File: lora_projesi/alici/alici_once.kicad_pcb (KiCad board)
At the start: 4 copper layers, 88 x 102 mm, 127 parts, among them J1 USB-C, J2 SMA, J3 RJ45, J4 u.FL (ANA ANTEN), J5 12 V GIRIS, J6 LAMBA, J7 MICRO-SIM, J8 u.FL (YARDIMCI ANTEN, ISTEGE 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, K1 SRD-12VDC-SL-A, Q1 AO3401A, Q2 MMBT2222A, Q3 MMBT2222A, Q4 MMBT2222A, SW1 DUGME, U1 ESP32-S3-WROOM-1-N4, U10 SIM7600SA, U11 AP2112K-3.3, U12 ESDA6V1-5SC6, U4 RFM95W-915S2, U5 TPS62933DRLR, U6 TPS62933DRLR, U7 USBLC6-2SC6, U8 TXB0104PW, U9 W5500, Y1 25 MHz

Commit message: A7670SA, Ra-01H, LM66100 ideal diyot, SRP7028A, USBLC6-2: uretec ve kutuphane (kart yonlendirmesi suruyor)
Co-Authored-By: Claude Sonnet 5.5 <noreply@anthropic.com>
Claude-Session: https://claude.ai/code/session_01Q71gHQtKJ86ZE2CtYTYSwP
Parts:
- removed D4: SS14, D_SMA
- removed J8: u.FL (YARDIMCI ANTEN, ISTEGE BAGLI), U.FL_Hirose_U.FL-R-SMT-1_Vertical
- removed R36: 0, R_0603_1608Metric
- added C52: 33pF, C_0603_1608Metric, B.Cu at (37.8, 52.9)
- added C53: 10pF, C_0603_1608Metric, B.Cu at (41.7, 49.1)
- added C54: 1uF, C_0603_1608Metric, B.Cu at (43.6, 50.0)
- added R39: 22, R_0603_1608Metric, B.Cu at (17.8, 54.0)
- added R40: 22, R_0603_1608Metric, B.Cu at (16.0, 52.0)
- added R41: 22, R_0603_1608Metric, B.Cu at (15.1, 50.1)
- added TP4: USB_VBUS, TestPoint_Pad_1.0x1.0mm, F.Cu at (11.2, 47.6)
- added TP5: UART_LOG_TX, TestPoint_Pad_1.0x1.0mm, F.Cu at (10.6, 44.5)
- added U13: USBLC6-2SC6, SOT-23-6, F.Cu at (40.2, 27.5)
- added U14: USBLC6-2SC6, SOT-23-6, B.Cu at (25.2, 57.4)
- added U15: LM66100, SOT-363_SC-70-6, F.Cu at (5.14, 89.1)
- C12, C5: value 100nF 25V -> 100nF 25V X7R
- C16: value 330uF 6,3V polimer -> 330uF 6,3V polimer ESR en fazla 40 mOhm
- C44, C45: value 100nF -> 1nF
- F1: value 1812L200 (2 A) -> 1812L200/16DR (2 A, 16 V)
- L1, L2: value 4,7uH 5A -> 4,7uH Isat 10A; footprint L_Bourns-SRN6028 -> L_Bourns_SRP7028A_7.3x6.6mm
- R4: value 37,4k 1% -> 40,2k 1%
- TP1: value BOOT_CFG0 -> USB_BOOT
- TP2: value USB_DN -> USB_DM
- U10: value SIM7600SA -> A7670SA; footprint SIM7600_LCC87 -> A7670SA_LGA88
- U12: value ESDA6V1-5SC6 -> USBLC6-2SC6
- U4: value RFM95W-915S2 -> Ra-01H; footprint HOPERF_RFM9XW_SMD -> Ra-01H
- moved C1 36.1 mm to (8.63, 32.9)
- moved R38 35.1 mm to (38.9, 2.01)
- moved R32 34.8 mm to (39.5, 31.1)
- moved C44 32.8 mm to (41.4, 32.0), turned to 90 degrees
- moved R37 30.2 mm to (30.5, 1.47), turned to 0 degrees
- moved R31 30.2 mm to (35.9, 28.7)
- moved D7 30.1 mm to (34.7, 17.0), turned to 90 degrees
- moved Q2 29.8 mm to (35.0, 2.96)
- moved Q3 27.8 mm to (36.3, 32.0), turned to 0 degrees
- moved TP1 25.4 mm to (20.7, 32.5)
- moved C2 20.7 mm to (16.7, 31.3)
- moved D2 20.3 mm to (17.6, 28.0), turned to 0 degrees
- moved C26 17.9 mm to (40.0, 61.4), turned to 0 degrees
- moved C27 17.8 mm to (36.0, 61.8)
- moved R19 17.6 mm to (47.4, 54.2)
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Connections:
- TP1 pad 1: BOOT_CFG0 -> USB_BOOT
- U10 pad 1: GND -> PWRKEY
- U10 pad 10: GND -> M_RXD
- U10 pad 12: M_USB_DN -> (no net)
- U10 pad 13: M_USB_DP -> (no net)
- U10 pad 14: GND -> (no net)
- U10 pad 16: (no net) -> MODEM_RESET
- U10 pad 17: USIM_DATA -> GND
- U10 pad 18: USIM_RST -> GND
- U10 pad 19: USIM_CLK -> (no net)
- U10 pad 20: USIM_VDD -> (no net)
- U10 pad 23: (no net) -> LOG_TX
- U10 pad 24: (no net) -> M_USB_VBUS
- U10 pad 27: (no net) -> M_USB_DP
- U10 pad 28: (no net) -> M_USB_DN
- U10 pad 29: (no net) -> GND
- U10 pad 3: PWRKEY -> (no net)
- U10 pad 30: (no net) -> USIM_VDD
- U10 pad 31: (no net) -> USIM_DATA_M
- U10 pad 32: (no net) -> USIM_CLK_M
- U10 pad 33: (no net) -> USIM_RST_M
- U10 pad 37: GND -> (no net)
- U10 pad 38: VBAT_MOD -> (no net)
- U10 pad 39: VBAT_MOD -> GND
- U10 pad 4: MODEM_RESET -> (no net)
- U10 pad 40: GND -> (no net)
- U10 pad 41: GND -> (no net)
- U10 pad 43: GND -> (no net)
- U10 pad 45: (no net) -> GND
- U10 pad 46: (no net) -> GND
- U10 pad 49: M_STATUS -> (no net)
- U10 pad 5: GND -> (no net)
- U10 pad 54: (no net) -> GND
- U10 pad 55: (no net) -> VBAT_MOD
- U10 pad 56: (no net) -> VBAT_MOD
- U10 pad 57: GND -> VBAT_MOD
- U10 pad 59: MODEM_AUX -> GND
- U10 pad 6: (no net) -> USB_BOOT
- U10 pad 60: GND -> MODEM_ANT
- U10 pad 62: VBAT_MOD -> GND
- U10 pad 63: VBAT_MOD -> GND
- U10 pad 66: (no net) -> M_STATUS
- U10 pad 68: M_RXD -> (no net)
- U10 pad 69: (no net) -> GND
- U10 pad 70: (no net) -> GND
- U10 pad 71: M_TXD -> GND
- U10 pad 72: (no net) -> GND
- U10 pad 73: (no net) -> GND
- U10 pad 74: (no net) -> GND
- U10 pad 75: (no net) -> GND
- U10 pad 76: (no net) -> GND
- U10 pad 79: (no net) -> GND
- U10 pad 82: MODEM_ANT -> GND
- U10 pad 83: (no net) -> GND
- U10 pad 84: (no net) -> GND
- U10 pad 85: BOOT_CFG0 -> GND
- U10 pad 86: (no net) -> GND
- U10 pad 87: (no net) -> GND
- U10 pad 9: (no net) -> M_TXD
- U12 pad 4: USIM_DATA -> USIM_CLK
- U12 pad 6: (no net) -> USIM_RST
- U4 pad 1: GND -> ANT_RF
- U4 pad 10: GND -> (no net)
- U4 pad 12: (no net) -> SPI_SCK
- U4 pad 13: +3V3 -> SPI_MISO
- U4 pad 14: LORA_DIO0 -> SPI_MOSI
- U4 pad 15: LORA_DIO1 -> LORA_NSS
- U4 pad 16: (no net) -> GND
- U4 pad 2: SPI_MISO -> GND
- U4 pad 3: SPI_MOSI -> +3V3
- U4 pad 4: SPI_SCK -> LORA_RESET
- U4 pad 5: LORA_NSS -> LORA_DIO0
- U4 pad 6: LORA_RESET -> LORA_DIO1
- U4 pad 8: GND -> (no net)
- U4 pad 9: ANT_RF -> GND
- U8 pad 10: (no net) -> GND
- U8 pad 5: (no net) -> GND
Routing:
- net GND: track 113.5 -> 141.9 mm, vias 119 -> 141
- net +3V3: track 26.7 -> 26.6 mm, vias 25 -> 26

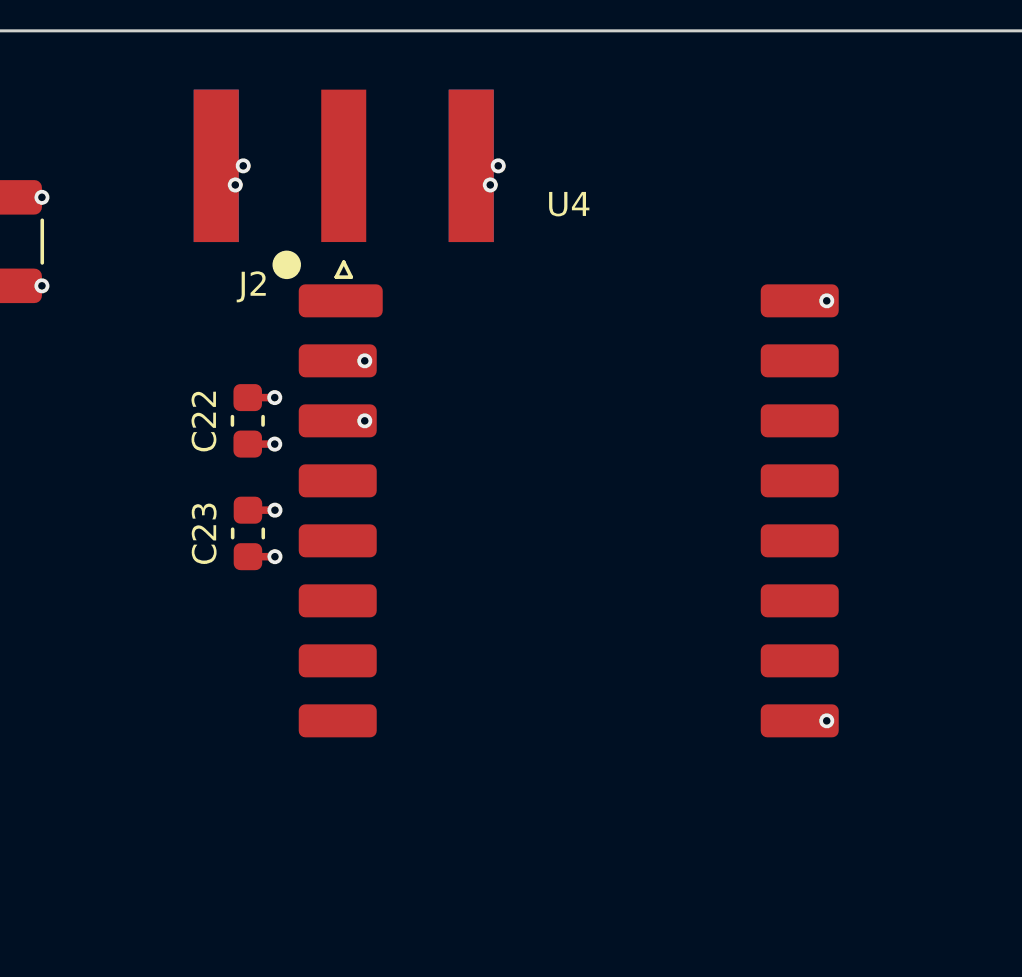
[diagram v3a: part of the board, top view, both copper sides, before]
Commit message: Verici Ra-01H ile yonlendirildi (DRC hata 0); maliyet modeli LCSC fiyatlarina guncellendi; alici yonlendirmesi suruyor
Co-Authored-By: Claude Sonnet 5.5 <noreply@anthropic.com>
Claude-Session: https://claude.ai/code/session_01Q71gHQtKJ86ZE2CtYTYSwP
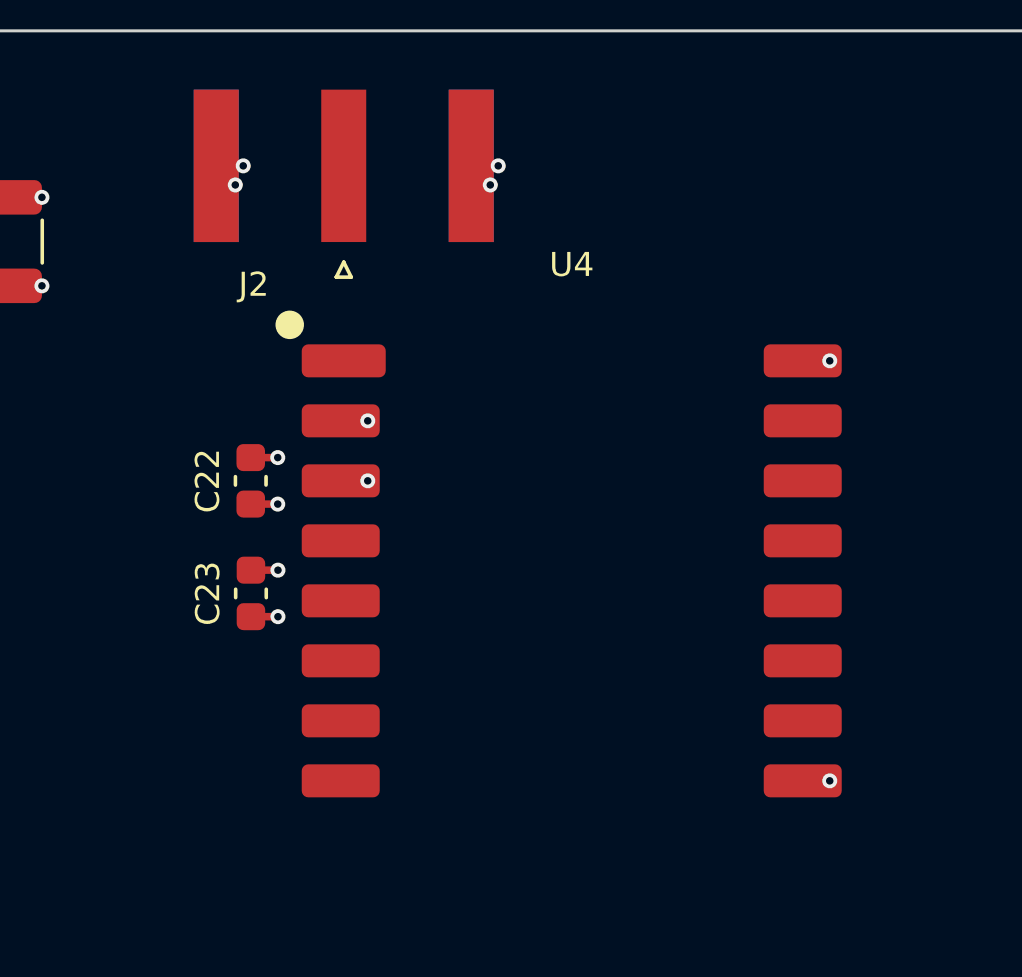
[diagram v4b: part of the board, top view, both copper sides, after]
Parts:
- moved C22 2.00 mm to (59.4, 15.0)
- moved C23 2.00 mm to (59.4, 18.8)
- moved U4 2.00 mm to (70.1, 18.0)
